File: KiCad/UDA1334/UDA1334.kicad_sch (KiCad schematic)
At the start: 32 parts, among them U1 UDA1334ATS, U2 MIC5225-3.3

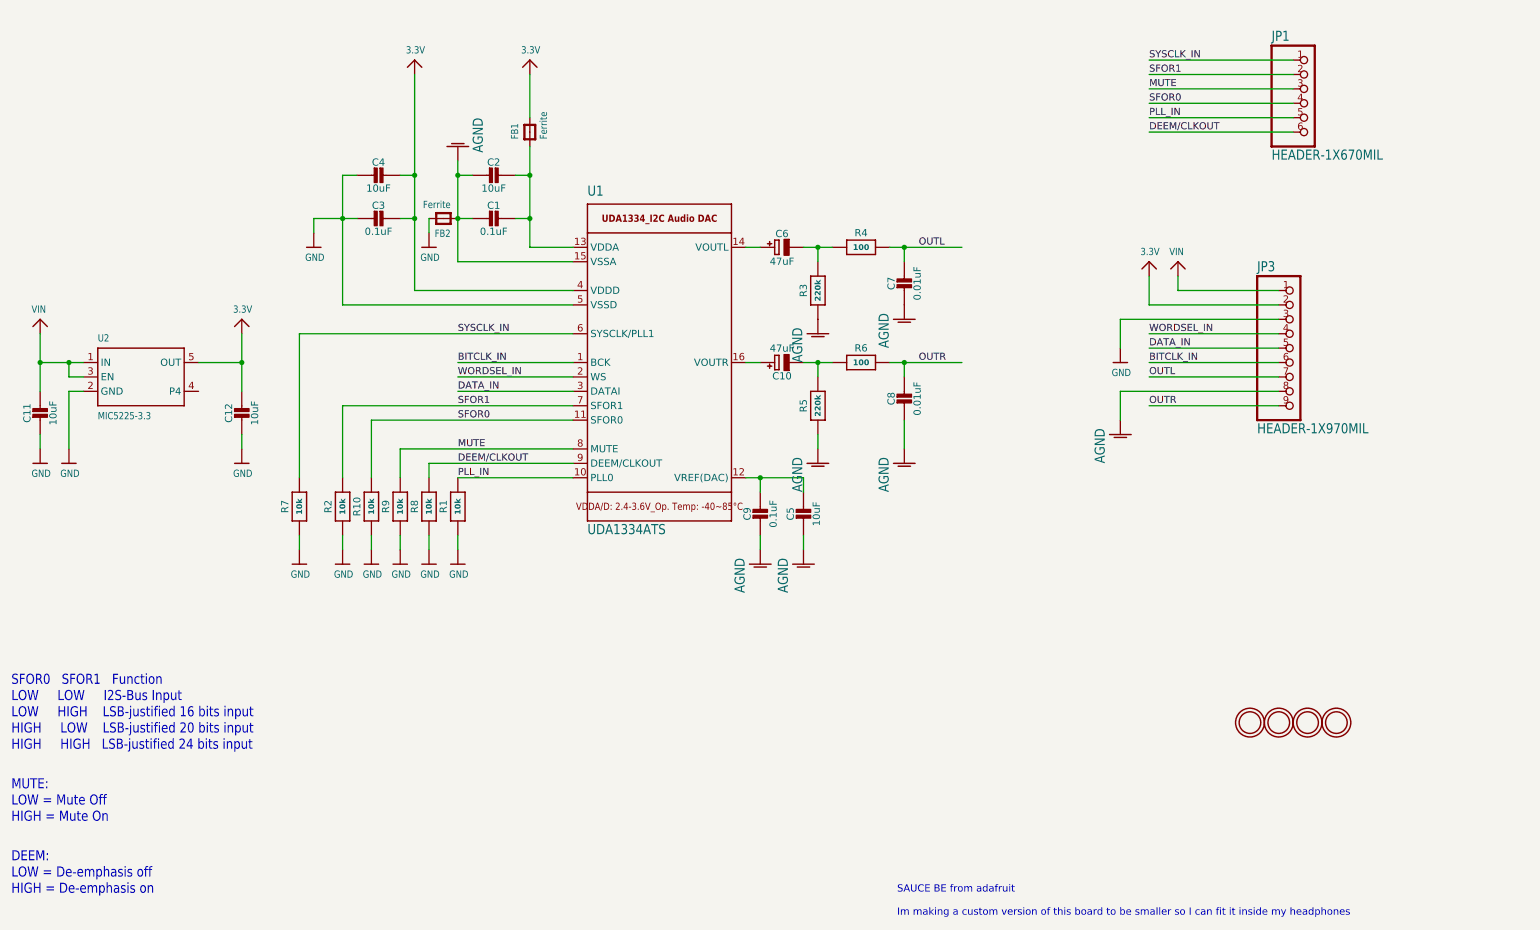
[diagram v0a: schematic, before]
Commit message: started swapping symbols from eagle import to KiCad
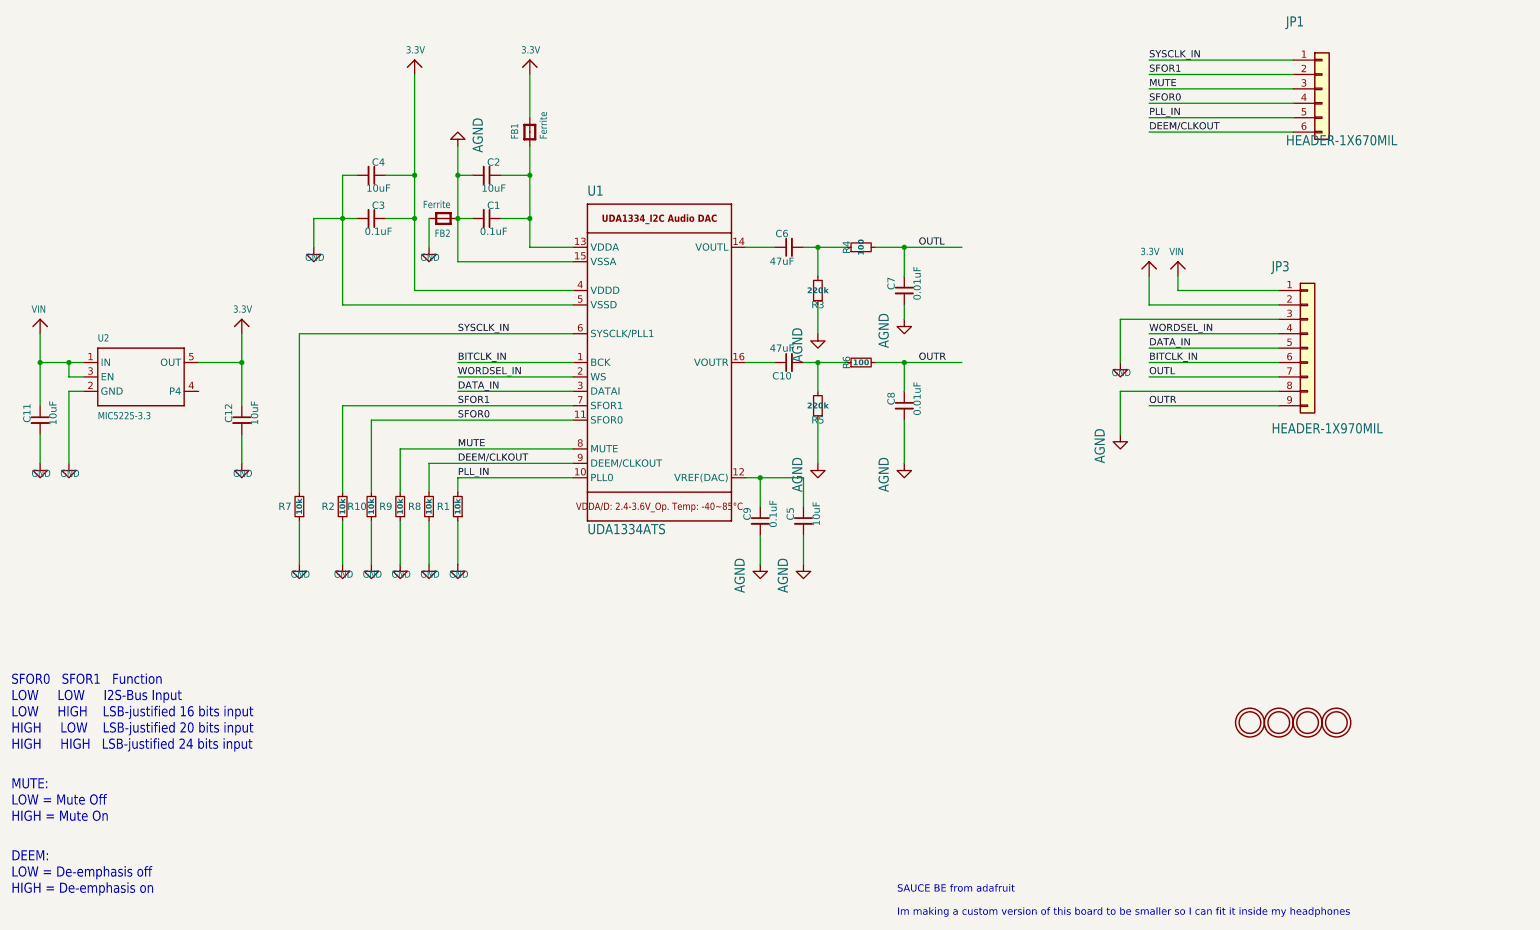
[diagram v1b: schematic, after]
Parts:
- C1, C11, C12, C2, C3, C4, C5, C7, C8, C9: symbol UDA1334-eagle-import:CAP_CERAMIC0805-NOOUTLINE -> Device:C_Small
- C10, C6: symbol UDA1334-eagle-import:CAP_ELECTROLYTICPANASONIC_C -> Device:C_Small
- JP1: symbol UDA1334-eagle-import:HEADER-1X670MIL -> Connector_Generic:Conn_01x06
- JP3: symbol UDA1334-eagle-import:HEADER-1X970MIL -> Connector_Generic:Conn_01x09
- R1, R10, R2, R7, R8, R9: symbol UDA1334-eagle-import:RESISTOR_0603_NOOUT -> Device:R_Small
- R3, R4, R5, R6: symbol UDA1334-eagle-import:RESISTOR0805_NOOUTLINE -> Device:R_Small
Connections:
- net GND: now also R2.2; no longer R2.1
- net SFOR1: now also R2.1; no longer R2.2
- net at R3.2, R4.1: now also C6.2; no longer C6.-
- net at R5.2, R6.1: now also C10.2; no longer C10.-
- net at U1.14 (VOUTL): now also C6.1; no longer C6.+
- net at U1.16 (VOUTR): now also C10.1; no longer C10.+
- net AGND renamed GNDA
